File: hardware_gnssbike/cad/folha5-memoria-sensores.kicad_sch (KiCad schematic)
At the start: 16 parts, among them U501 MX25R6435F, U502 Bosch BMP585, U503 Bosch BMI270, U504 Memsic MMC5603NJ, U505 TI OPT3001DNPR

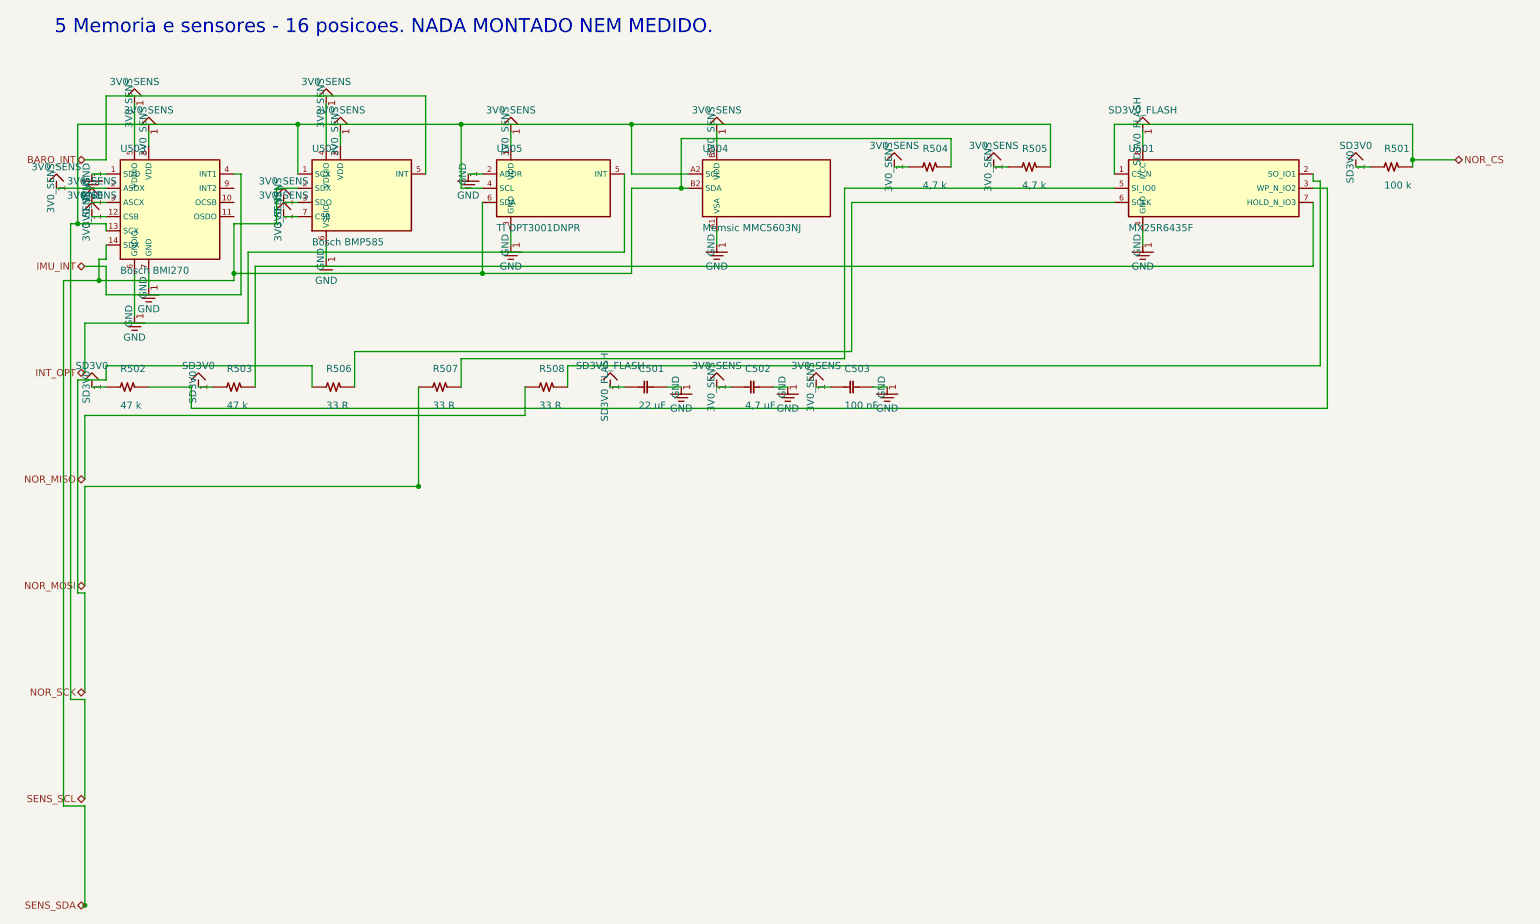
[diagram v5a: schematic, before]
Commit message: fix(hardware): the debug connector had RESET on the wrong contact
This one would have cost a board. The Tag-Connect TC2030 footprint had
pin 3 as no-connect and RESET on pin 6. The manufacturer's own data
sheet, TC2030-CTX_1.pdf, table "Connections", says the opposite: on the
six-pin footprint it is 3 = nRESET and 6 = SWO/TDO.

Where the mistake came from is worth writing down, because it is easy to
make twice: 1 VCC, 2 SWDIO, 3 GND, 4 SWCLK, 5 GND, 6 SWO is the
numbering of the ten-way Cortex header on the PROBE side, not of the
six-pin footprint on the board. Mixing the two gives exactly what was
written here.

What it would have done: the probe's nRESET is an open drain output, so
it would have driven nothing, and the MCU's reset would have hung off
the probe's SWO INPUT. Nothing burns - SWO runs target to probe, there
is no short - but the debugger can never reset the target: no connect
under reset, no pin reset. On an nRF54LM20A that reboots from task_wdt
or reconfigures its SWD pins, that removes the standard way out and
leaves only a full CTRL-AP erase.

The documentation carried a worse version still. 06 had GND on contact 3,
which fabricated would tie the probe's open-drain nRESET to copper
ground and hold the target in reset forever.

The project's own notes had predicted this exact variant - 06 carried a
CAUTION saying so and README an open checklist item. It was that one, and
it was caught before layout. Both are now closed, and the connector's
pin 6 is recorded as SWO with what is still unknown about it: which pad
of the ME54BS13 exposes SWO, which would give printf over ITM during
bring-up.

Fixed in parts.py, nets.py, 03-netlist.md, 06-conectores-e-pontos-de-teste.md,
07-sequencias-e-protecao.md and README.md.

Verified: check_sch and check_pcb pass, 78 of 78 diagrams render, 1529
links and none broken.
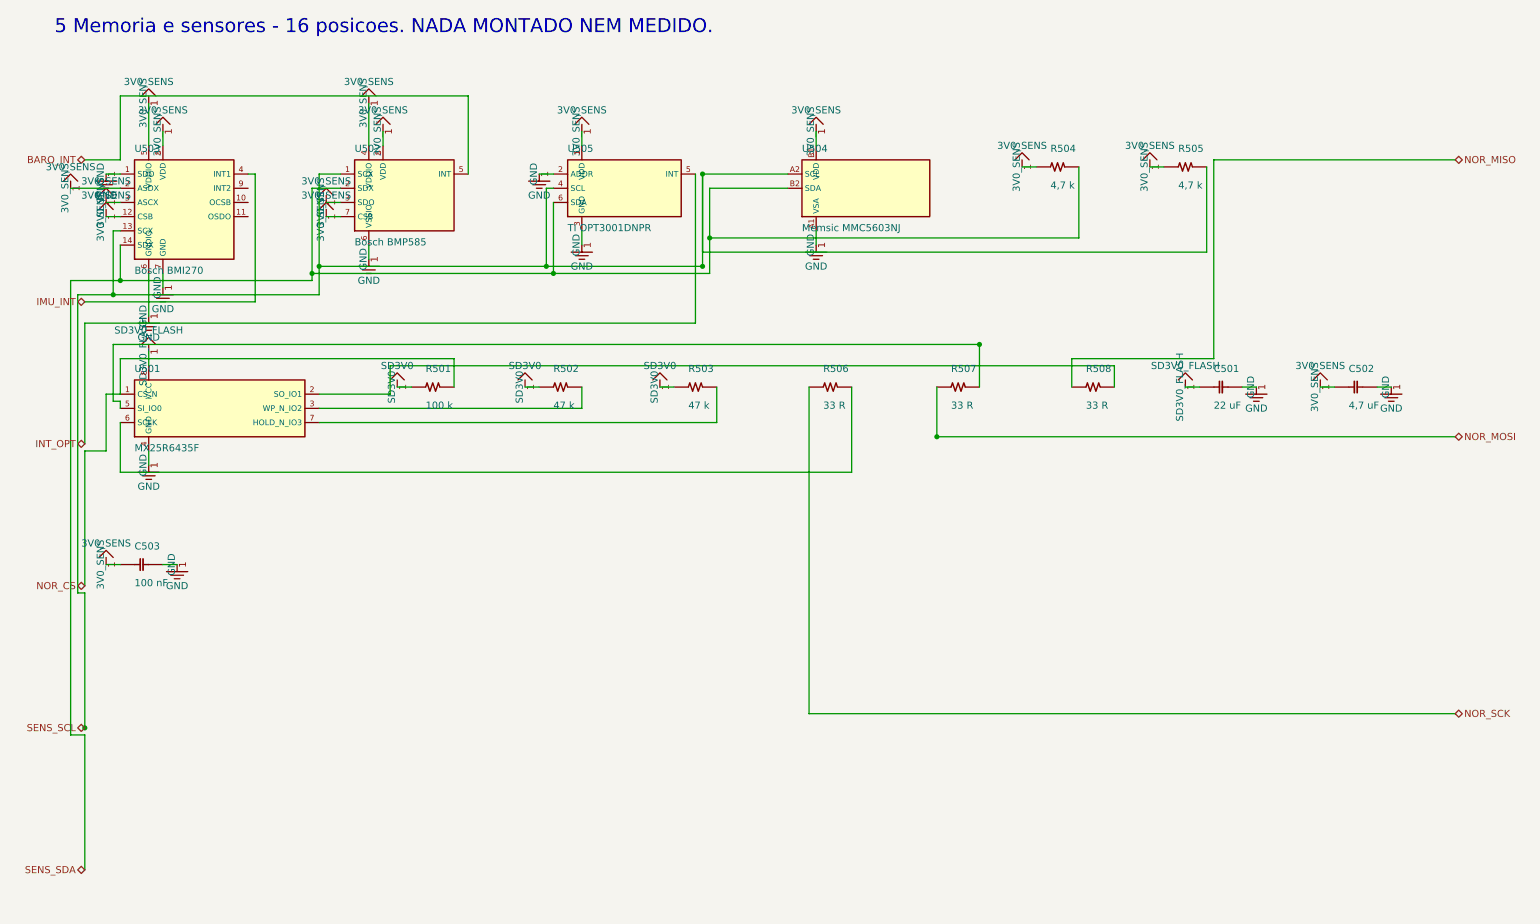
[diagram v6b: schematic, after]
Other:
- moved on the sheet: C501, C502, C503, R501, R502, R503, R504, R505, R506, R507, R508, U501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

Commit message: feat(hardware): the ERC runs, and 52 hidden errors became 4 deliberate ones
check_sch.py compared our netlist against the one KiCad extracts, pin by
pin, and was good at that and blind to everything else. KiCad's own ERC
had never been run on this schematic. It found 52 errors, and among them
a capacitor with BOTH terminals in the air.

They were of four kinds, and three of them were the drawing failing to
say what it meant rather than the circuit being wrong:

  34 open pins with no flag. The NC pins of the ESD array, the GPIOs
  nobody uses, the receiver's SDA and SCL - it speaks UART - the
  programmer's SWO. Every one of them deliberate, and indistinguishable
  from a forgotten wire. They now carry a no-connect flag, taken from
  nets.py, which is already the source of truth about what is open: a
  pin that appears in no net is open, full stop. A net with a single pin
  counts as open too, which is what R111 became when the harvester
  changed and its pull-up lost its job.

  12 rails with no source the ERC could see. The 1V8_GNSS comes from
  1V8 through a ferrite, the SD3V0_FLASH from SD3V0 through a jumper,
  the harvester's VIN from the panel. PWR_FLAG is the symbol that exists
  to say "this is supplied, I answer for it". One per ELECTRICAL GROUP,
  not per net and not per sheet: two nets that share a pin are one net
  to KiCad - the display connector carries FPC_VSS on one side and GND
  on the other through the same contact - and a flag on each side would
  be two supply outputs wired together, which is another error.

  The last one needed the electrical type to come from the symbol that
  actually reaches the sheet. The four VBUS contacts of the USB-C are
  power_out in our parts.py and passive in KiCad's symbol, so the rule
  believed the rail had a source when it had none.

What is left is four violations, and all four are the same thing: two
supply OUTPUTS wired together. KiCad calls that an error by default
because in signal circuitry two outputs on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
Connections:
- no-connect marks 0 -> 3
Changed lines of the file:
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@@
 		(stroke (width 0) (type default))
+	)
+	(no_connect
+		(at 54.610 39.370)
+	)
+	(no_connect
+		(at 54.610 41.910)
+	)
+	(no_connect
+		(at 54.610 44.450)
 	)
 	(junction

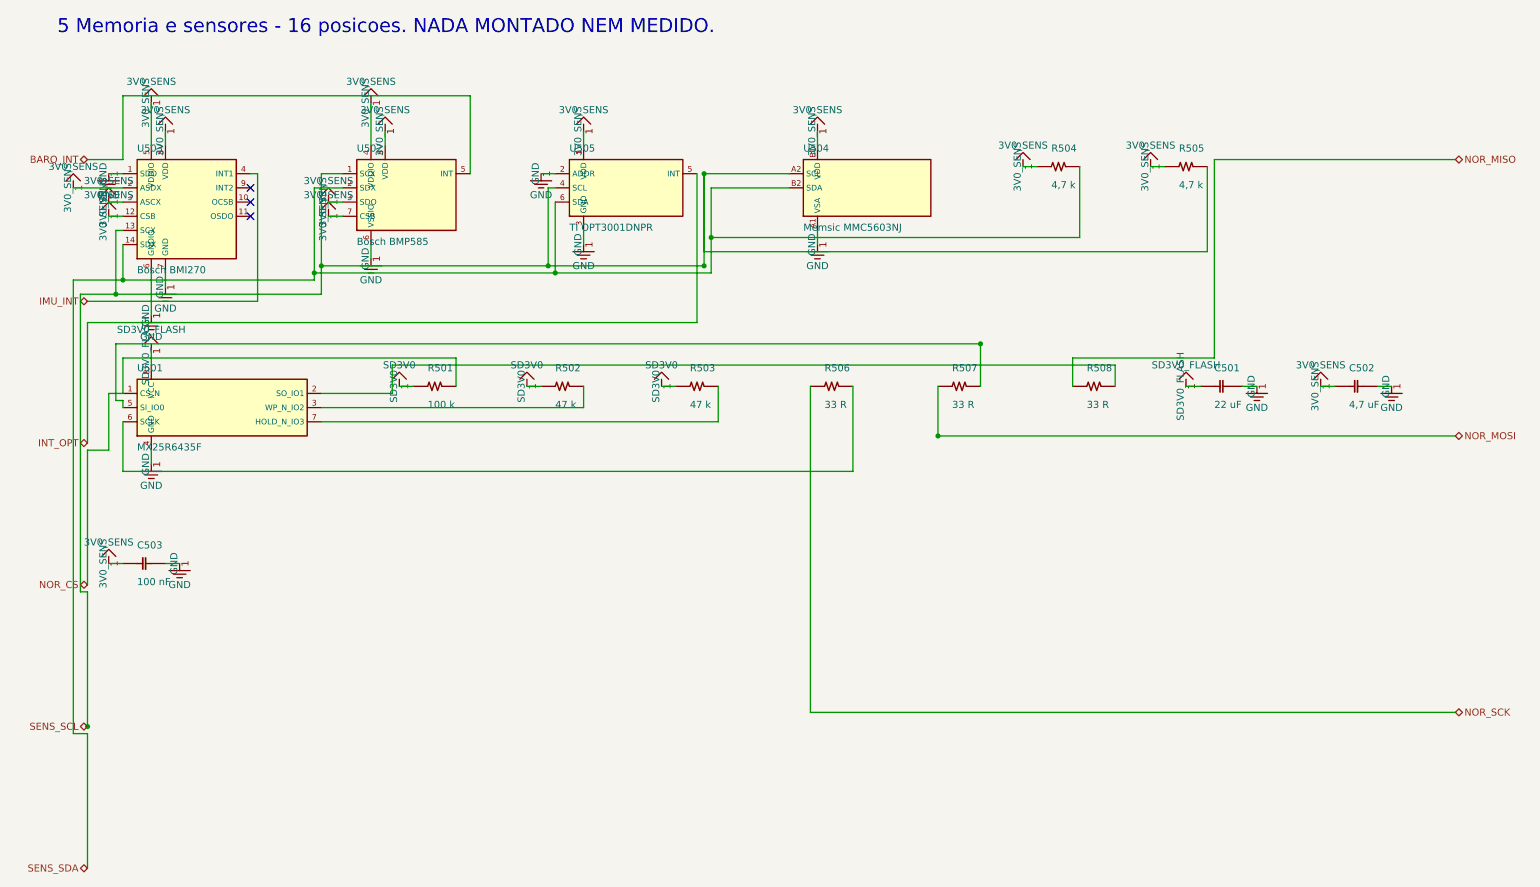
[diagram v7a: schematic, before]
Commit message: feat(hardware): draw the schematic by functional block, the way a person reads it
The owner asked for an industrial-standard schematic: wires and labels,
A4 or A3 pages, the right symbols and values, easy to read, the circuits
subdivided by dashed boxes. Until now each sheet was the netlist drawn as
wires - parts on a grid in connection order and a maze router pulling a
wire from every pin to wherever its other end was, across the page.

blocos.py turns each sheet into a row of functional blocks in the order
the signal flows, each in a dashed rectangle with a title: on the power
sheet, USB-C and protection, the nPM1300, the gauge and the cell, the GNSS
backup, the solar harvester, the thermal cut-off. Membership comes from
the BLOCOS table (the anchors), then make_pcb.DECOPLA and JUNTO (the
board already says whose each capacitor is), then sheets.SEGUE, then the
netlist without rails, nearest anchor by hops. Inside a block the anchor
sits in the middle and each passive beside the pin it serves, on the
side that pin faces, mirrored when the pin that serves the chip is the
far one; parts that touch only rails go to a shelf under the chip. Rails
are power symbols, neighbouring pins of one rail get a wire along their
tips and one symbol; a net that leaves its block is a local label, one
that leaves the sheet a hierarchical label, both on a short stub the
maze router bends when the straight way is taken. Sheet 1 is A3, the
rest A4, measured by the drawing itself. Decoupling capacitors now live
on their chip's sheet whatever their number.

Three KiCad 8 facts were measured with kicad-cli's netlist export on the
way, because the first version assumed each one wrong and check_sch.py
caught it: (mirror x) swaps left for right, not (mirror y); a local label
named after a rail is the net /sheet/RAIL, another net; and a pin in the
middle of a long wire is not on it - "wires connect with other wires or
pins only if their ends coincide exactly" (Eeschema manual). The
conventions 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
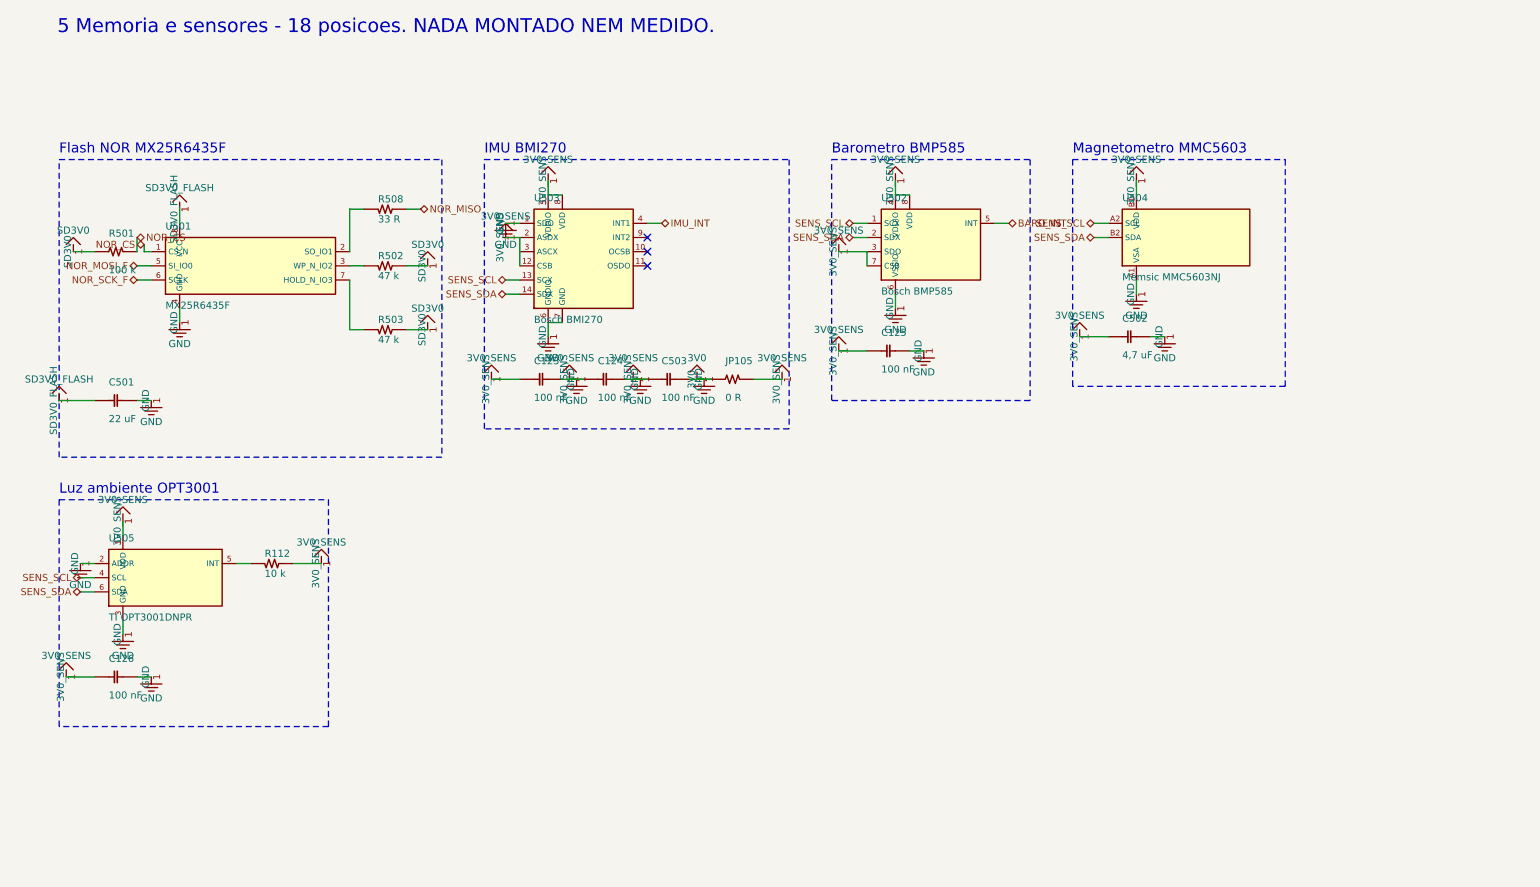
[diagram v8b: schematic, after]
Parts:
- removed R504: 4,7 k, Resistor_SMD:R_0402_1005Metric, symbol gnssbike:R504
- removed R505: 4,7 k, Resistor_SMD:R_0402_1005Metric, symbol gnssbike:R505
- removed R506: 33 R, Resistor_SMD:R_0402_1005Metric, symbol gnssbike:R506
- removed R507: 33 R, Resistor_SMD:R_0402_1005Metric, symbol gnssbike:R507
- added C123: 100 nF, Capacitor_SMD:C_0603_1608Metric, symbol gnssbike:C123
- added C124: 100 nF, Capacitor_SMD:C_0603_1608Metric, symbol gnssbike:C124
- added C125: 100 nF, Capacitor_SMD:C_0603_1608Metric, symbol gnssbike:C125
- added C126: 100 nF, Capacitor_SMD:C_0603_1608Metric, symbol gnssbike:C126
- added JP105: 0 R, Resistor_SMD:R_0402_1005Metric, symbol gnssbike:JP105
- added R112: 10 k, Resistor_SMD:R_0402_1005Metric, symbol gnssbike:R112
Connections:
- net GND is gone; now on net 3V0: C501.2, C502.2, C503.2, U501.4 (GND), U502.6 (VSSIO), U503.1 (SDO), U503.6 (GNDIO), U503.7 (GND), U504.A1 (VSA), U505.2 (ADDR), U505.3 (GND)
- net NOR_SCK_F: now reaches U501.6 (SCLK)
- net NOR_MOSI_F: now reaches U501.5 (SI_IO0)
- net 3V0_SENS renamed 3V0
- net 3V0: now also C123.1, C123.2, C124.1, C124.2, C125.1, C125.2, C126.1, C126.2, JP105.1, JP105.2, R112.1
- net INT_OPT: no longer names the net of U505.5 (INT)
- net INT_OPT: now also R112.2
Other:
- note added: "5 Memoria e sensores - 18 posicoes. NADA MONTADO NEM MEDIDO."
- note added: "Barometro BMP585"
- note added: "Flash NOR MX25R6435F"
- note added: "IMU BMI270"
- note added: "Luz ambiente OPT3001"
- note added: "Magnetometro MMC5603"
- note removed: "5 Memoria e sensores - 16 posicoes. NADA MONTADO NEM MEDIDO."
- moved on the sheet: C501, C502, C503, R501, R502, R503, R508, U501, U502, U503, U504, U505
